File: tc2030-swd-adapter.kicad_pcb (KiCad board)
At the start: 2 copper layers, 38.2 x 34.5 mm, 15 parts, among them J1 TC2030, J2 JLINK-Interface, J3 Conn_01x03, J4 Conn_01x02, J5 TC2030, SW1 B3U-1000P, U1 RT9080-33GJ5

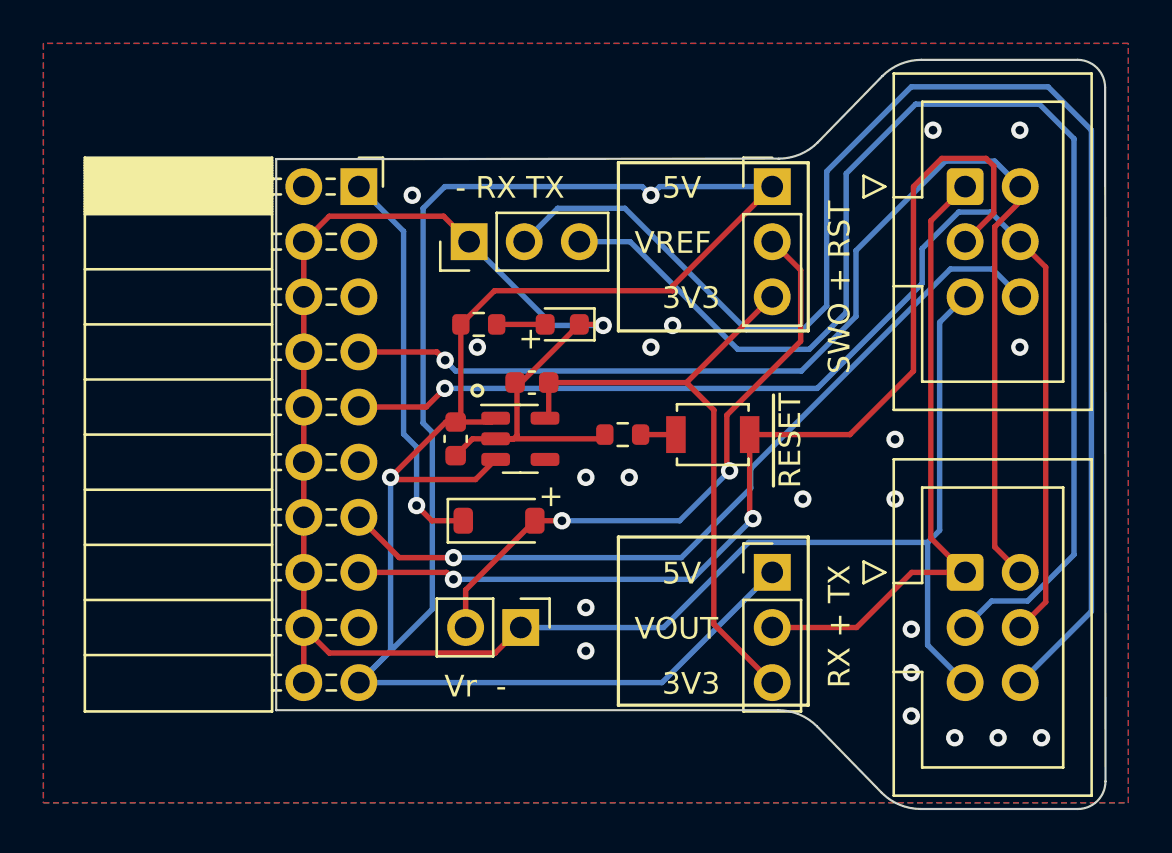
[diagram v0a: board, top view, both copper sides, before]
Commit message: Add UART to JLINK
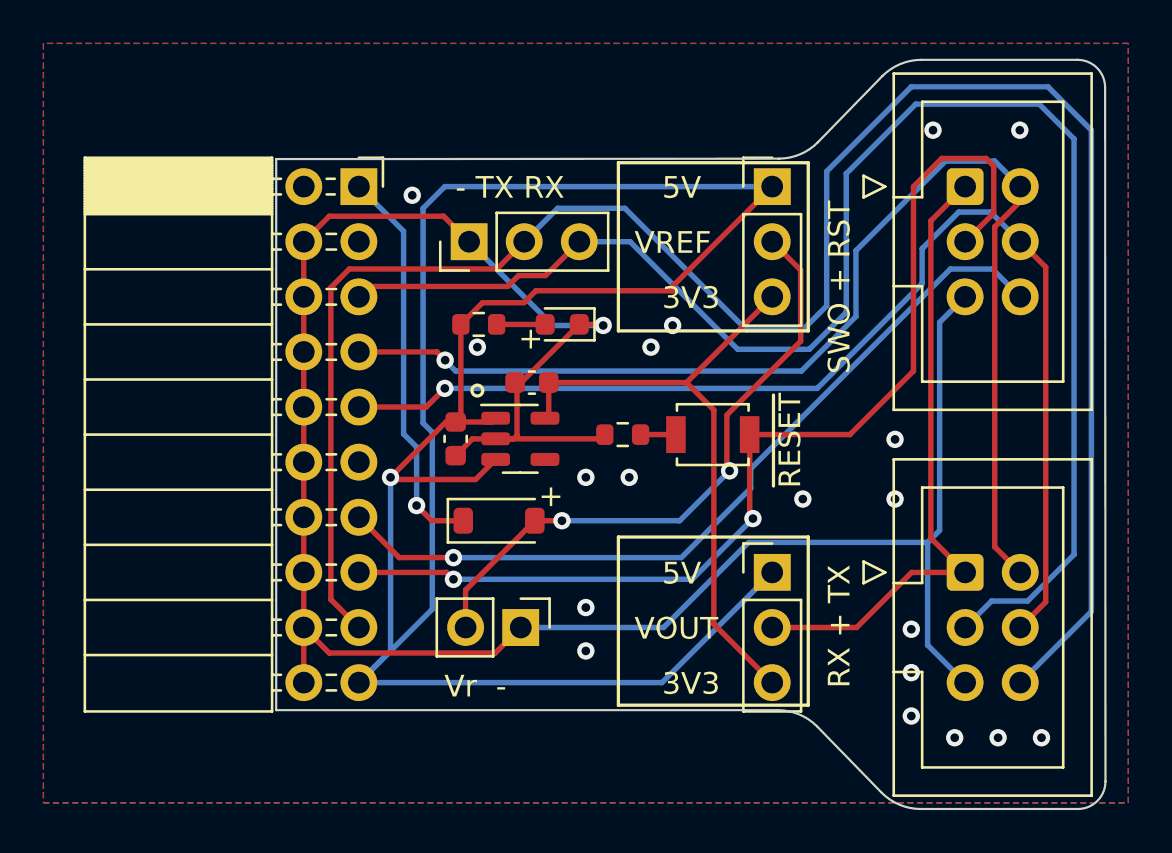
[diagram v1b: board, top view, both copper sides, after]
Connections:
- J2 pad 17: unconnected-(J2-Pin_17-Pad17) -> /JLINK_RX
- J2 pad 5: unconnected-(J2-Pin_5-Pad5) -> /JLINK_TX
- J3 pad 2: /TX -> /JLINK_RX
- J3 pad 3: /RX -> /JLINK_TX
- J5 pad 3: /RX -> /JLINK_TX
- J5 pad 6: /TX -> /JLINK_RX
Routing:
- net /JLINK_RX: track 0.00 -> 91.0 mm
- net /JLINK_TX: track 0.00 -> 70.7 mm
- net /TX: track 65.0 -> 0.00 mm
- net /RX: track 59.5 -> 0.00 mm
- net +5V: track 104.4 -> 104.1 mm, vias 2 -> 1
- net GND: vias 21 -> 20
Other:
- board text added: "- TX RX"
- board text removed: "- RX TX"
